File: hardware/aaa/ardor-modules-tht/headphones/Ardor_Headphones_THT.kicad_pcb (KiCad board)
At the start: 2 copper layers, 96 x 84 mm, 38 parts, among them J101 5V POWER + ENABLE INPUT, J102 STEREO AUDIO INPUT FROM SOURCE, J602 STEREO HEADPHONE AUDIO OUTPUT, K601 G5V-2-H1 DC5, Q601 2N3904 / E-B-C, U601 LM386N-1/NOPB, U602 LM386N-1/NOPB

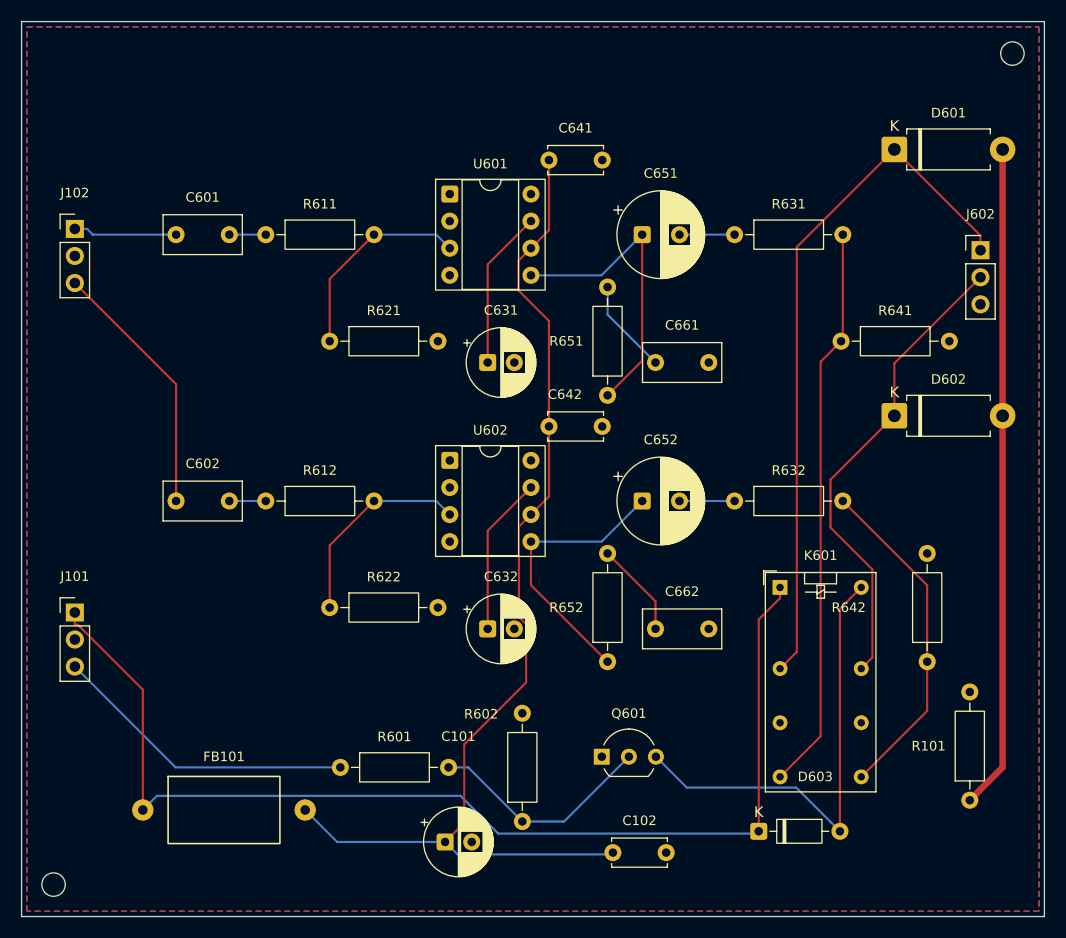
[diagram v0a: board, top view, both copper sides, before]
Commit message: feat(hardware): use hand-solderable OPA1656 headphone amplifier
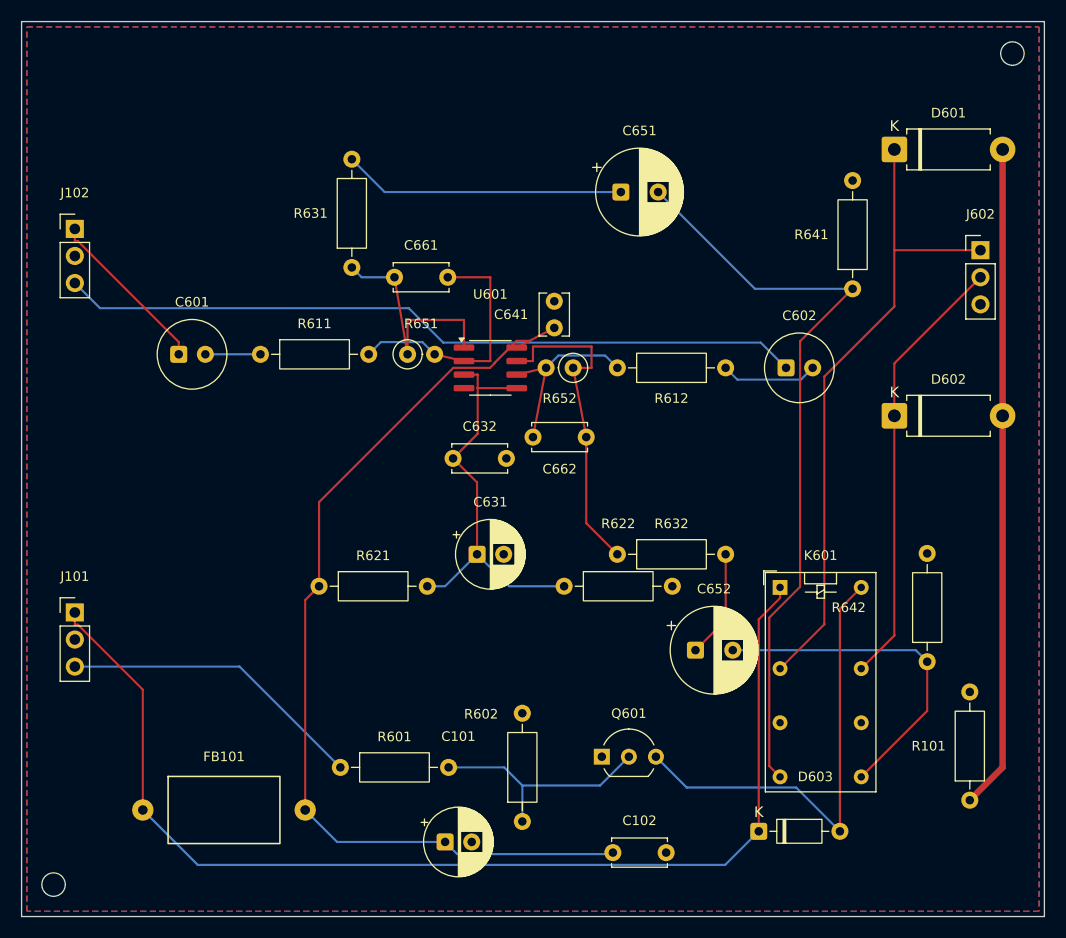
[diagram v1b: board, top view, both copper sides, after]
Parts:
- removed C642: 100n / 50V X7R, Capacitor_THT:C_Disc_D5.0mm_W2.5mm_P5.00mm
- removed U602: LM386N-1/NOPB, Package_DIP:DIP-8_W7.62mm_Socket
- C601, C602: value 1u / 63V FILM -> 10u / 25V BIPOLAR; footprint Capacitor_THT:C_Rect_L7.2mm_W3.5mm_P5.00mm_FKS2_FKP2_MKS2_MKP2 -> Ardor_THT:CP_Bipolar_D6.3mm_P2.50mm
- C631: value 10u / 25V -> 47u / 25V
- C632: value 10u / 25V -> 100n / 50V X7R; footprint Capacitor_THT:CP_Radial_D6.3mm_P2.50mm -> Capacitor_THT:C_Disc_D5.0mm_W2.5mm_P5.00mm
- C641: value 100n / 50V X7R -> 100n / 50V X7R / P2.5mm; footprint Capacitor_THT:C_Disc_D5.0mm_W2.5mm_P5.00mm -> Capacitor_THT:C_Disc_D3.8mm_W2.6mm_P2.50mm
- C661, C662: value 47n / 50V FILM -> 100p / 50V C0G; footprint Capacitor_THT:C_Rect_L7.2mm_W3.5mm_P5.00mm_FKS2_FKP2_MKS2_MKP2 -> Capacitor_THT:C_Disc_D5.0mm_W2.5mm_P5.00mm
- R611, R612: value 39k / 1% 0.25W -> 20k / 1% 0.25W
- R621, R622: value 1k / 1% 0.25W -> 10k / 1% 0.25W
- R631, R632: value 2.2R / 1% 0.25W -> 10R / 1% 0.25W
- R651, R652: value 10R / 1% 0.25W -> 10k / 1% 0.25W / UPRIGHT; footprint Resistor_THT:R_Axial_DIN0207_L6.3mm_D2.5mm_P10.16mm_Horizontal -> Resistor_THT:R_Axial_DIN0207_L6.3mm_D2.5mm_P2.54mm_Vertical
- U601: value LM386N-1/NOPB -> OPA1656ID; footprint Package_DIP:DIP-8_W7.62mm_Socket -> Package_SO:SOIC-8_3.9x4.9mm_P1.27mm
- moved C602 58.6 mm to (121.8, 82.5)
- moved R612 44.9 mm to (116.1, 82.5), turned to 180 degrees
- moved R631 36.1 mm to (81.0, 73.1), turned to 90 degrees
- moved R652 27.8 mm to (101.8, 82.5), turned to 180 degrees
- moved C661 25.8 mm to (85.0, 74.0)
- moved R621 23.0 mm to (77.9, 103.0)
- moved R622 22.1 mm to (100.9, 103.0)
- moved R651 19.2 mm to (86.2, 81.2), turned to 0 degrees
- moved C662 19.1 mm to (103.0, 89.0), turned to 180 degrees
- moved C631 18.0 mm to (92.8, 100.0)
- moved U601 16.7 mm to (94.0, 82.5)
- moved C632 16.3 mm to (90.5, 91.0)
- moved C641 15.8 mm to (100.0, 78.8), turned to 90 degrees
- moved C652 14.9 mm to (113.2, 109.0)
- moved R632 12.1 mm to (105.9, 100.0)
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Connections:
- C631 pad 1: Net-(U601-BYPASS) -> /VREF
- C632 pad 1: Net-(U602-BYPASS) -> /VREF
- C651 pad 2: Net-(C651-Pad2) -> /DRIVE_L
- C652 pad 2: Net-(C652-Pad2) -> /DRIVE_R
- C661 pad 2: /GND -> Net-(U601A--)
- C662 pad 2: /GND -> Net-(U601B--)
- R611 pad 2: Net-(U601-+) -> Net-(U601A--)
- R612 pad 2: Net-(U602-+) -> Net-(U601B--)
- R621 pad 1: Net-(U601-+) -> /+5V_A
- R621 pad 2: /GND -> /VREF
- R622 pad 1: Net-(U602-+) -> /VREF
- R631 pad 1: Net-(C651-Pad2) -> Net-(C661-Pad1)
- R631 pad 2: /DRIVE_L -> Net-(C651-Pad1)
- R632 pad 1: Net-(C652-Pad2) -> Net-(C662-Pad1)
- R632 pad 2: /DRIVE_R -> Net-(C652-Pad1)
- R651 pad 1: Net-(C651-Pad1) -> Net-(C661-Pad1)
- R651 pad 2: Net-(C661-Pad1) -> Net-(U601A--)
- R652 pad 1: Net-(C652-Pad1) -> Net-(C662-Pad1)
- R652 pad 2: Net-(C662-Pad1) -> Net-(U601B--)
- U601 pad 1: unconnected-(U601-GAIN-Pad1) -> Net-(C661-Pad1)
- U601 pad 2: /GND -> Net-(U601A--)
- U601 pad 3: Net-(U601-+) -> /VREF
- U601 pad 5: Net-(C651-Pad1) -> /VREF
- U601 pad 6: /+5V_A -> Net-(U601B--)
- U601 pad 7: Net-(U601-BYPASS) -> Net-(C662-Pad1)
- U601 pad 8: unconnected-(U601-GAIN-Pad8) -> /+5V_A
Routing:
- net Net-(J102-Pin_3): track 24.4 -> 70.0 mm
- net /VREF: track 0.00 -> 39.0 mm
- net Net-(U601A--): track 0.00 -> 24.3 mm
- net Net-(C662-Pad1): track 8.94 -> 30.9 mm
- net Net-(U602-+): track 19.4 -> 0.00 mm
- net Net-(U601-+): track 19.4 -> 0.00 mm
- net /DRIVE_L: track 53.3 -> 71.5 mm
- net Net-(U601B--): track 0.00 -> 17.1 mm
- net Net-(C652-Pad1): track 26.3 -> 10.2 mm
- net Net-(U602-BYPASS): track 15.0 -> 0.00 mm
- net Net-(U601-BYPASS): track 15.0 -> 0.00 mm
- net Net-(C661-Pad1): track 8.94 -> 22.8 mm
- net /+5V_A: track 101.6 -> 90.1 mm
- net Net-(J102-Pin_1): track 9.72 -> 16.0 mm
- net Net-(C602-Pad2): track 3.42 -> 9.09 mm
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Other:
- board text removed: "C642"
- board text removed: "U601.1 NC NO WIRE"
- board text removed: "U601.8 NC NO WIRE"
- board text removed: "U602"
- board text removed: "U602.1 NC NO WIRE"
- board text removed: "U602.8 NC NO WIRE"

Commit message: fix(hardware): use Hestore TVS diodes in hand-assembly modules
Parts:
- D601, D602: value SA5.0CA-E3/54 -> 1.5KE6.8CA; footprint Diode_THT:D_DO-15_P10.16mm_Horizontal -> Ardor_THT:D_TVS_DC_1.5KE_P15.24mm
- moved D602 5.44 mm to (127.4, 90.0)
- moved D601 5.18 mm to (127.4, 59.5)
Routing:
- net /HP_L: track 61.3 -> 71.7 mm
- net /CHASSIS: track 62.4 -> 65.1 mm
- net /HP_R: track 41.4 -> 43.7 mm
- net /+5V_A: track 90.1 -> 89.0 mm
- net /DRIVE_L: track 71.5 -> 70.6 mm
- net Net-(Q601-B): track 22.1 -> 21.5 mm

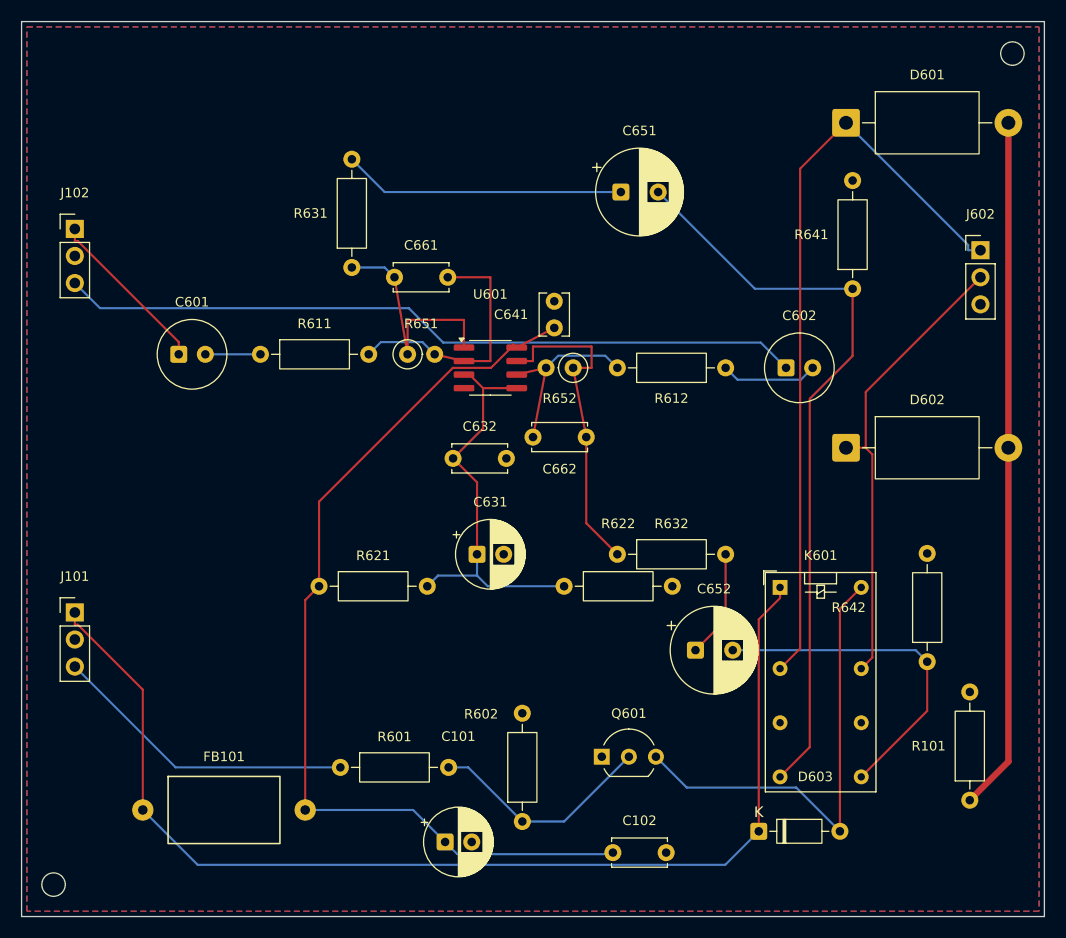
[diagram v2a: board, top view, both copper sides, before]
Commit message: feat(hardware): compact layouts and adopt Hestore module packages
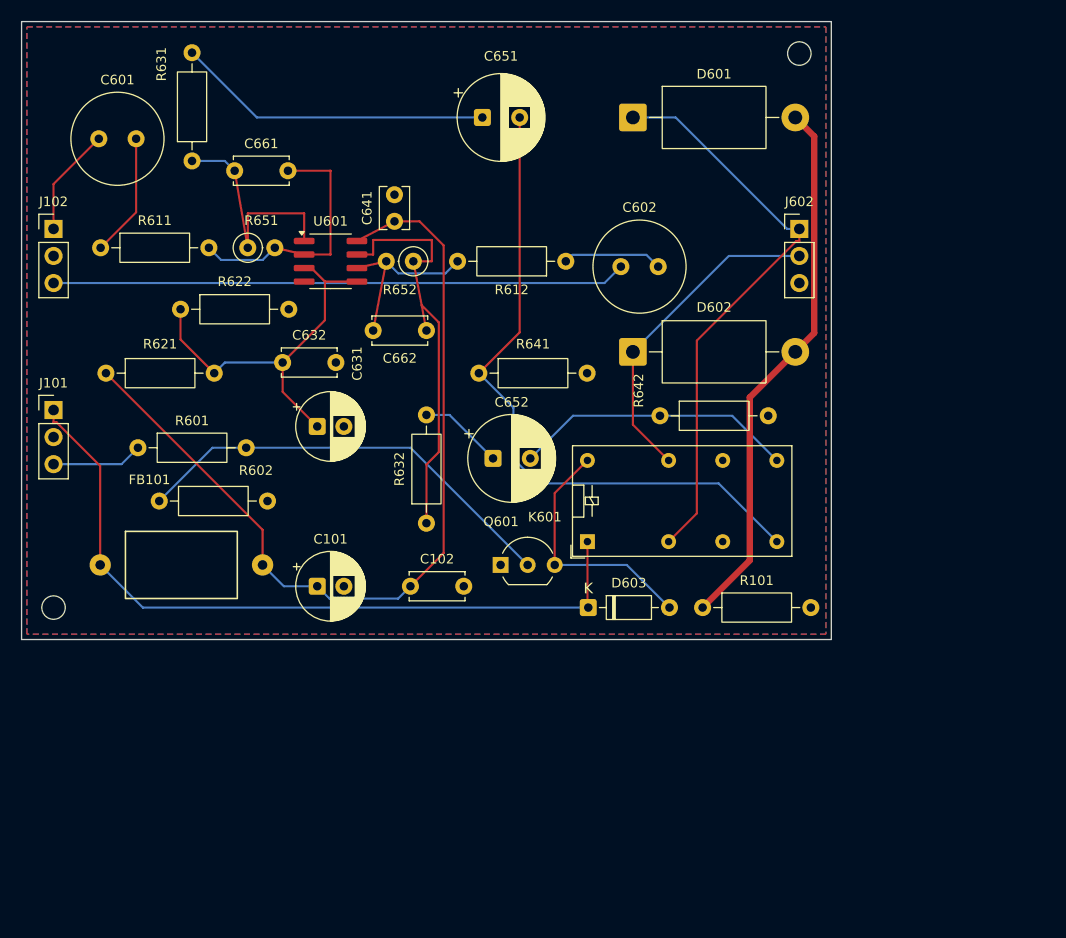
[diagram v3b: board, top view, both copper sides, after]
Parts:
- C601, C602: value 10u / 25V BIPOLAR -> 10u / 50V BIPOLAR; footprint Ardor_THT:CP_Bipolar_D6.3mm_P2.50mm -> Ardor_THT:CP_Bipolar_Nichicon_D8.0mm_P3.50mm
- moved R602 45.5 mm to (62.9, 95.0), turned to 0 degrees
- moved R622 44.4 mm to (64.9, 77.0)
- moved R641 36.0 mm to (92.9, 83.0), turned to 0 degrees
- moved R601 35.5 mm to (60.9, 90.0)
- moved R642 34.1 mm to (109.9, 87.0), turned to 0 degrees
- moved C102 31.4 mm to (86.5, 103.0)
- moved R101 30.9 mm to (113.9, 105.0), turned to 0 degrees
- moved R621 28.3 mm to (57.9, 83.0)
- moved C101 26.8 mm to (77.8, 103.0)
- moved D603 26.4 mm to (103.2, 105.0)
- moved C652 26.2 mm to (94.2, 91.0)
- moved H1 26.0 mm to (53.0, 105.0)
- moved FB101 23.3 mm to (57.4, 101.0)
- moved D602 21.9 mm to (107.4, 81.0)
- moved C601 21.6 mm to (57.2, 61.0)
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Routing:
- net /+5V: track 106.3 -> 70.2 mm
- net /RELAY_LOW: track 43.9 -> 23.5 mm
- net Net-(J101-Pin_3): track 28.8 -> 8.56 mm
- net Net-(Q601-B): track 21.5 -> 41.2 mm
- net /HP_L: track 71.7 -> 54.6 mm
- net Net-(J102-Pin_3): track 70.0 -> 53.9 mm
- net /CHASSIS: track 65.1 -> 51.1 mm
- net /HP_R: track 43.7 -> 30.9 mm
- net Net-(C662-Pad1): track 30.9 -> 40.3 mm
- net /DRIVE_L: track 70.6 -> 62.9 mm
- net Net-(C601-Pad2): track 5.17 -> 11.6 mm
- net /+5V_A: track 89.0 -> 82.6 mm
- net Net-(J102-Pin_1): track 16.0 -> 10.2 mm
- net /DRIVE_R: track 32.1 -> 26.5 mm
- net Net-(C651-Pad1): track 26.5 -> 29.8 mm
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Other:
- board size 96 x 84 mm -> 76 x 58 mm
